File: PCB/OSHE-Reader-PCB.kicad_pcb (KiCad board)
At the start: 2 copper layers, 85 x 90 mm, 74 parts, among them J1 UART, J2 112L-TDA0, J3 JTAG, J5 boot_select, Q1 Si1308EDL, Q2 BSS138, Q3 BSS138, U1 74LVC1G04, U2 TPS923610DRLR, U3 TLV75533PDBV, U4 ESP32-S3-WROOM-1

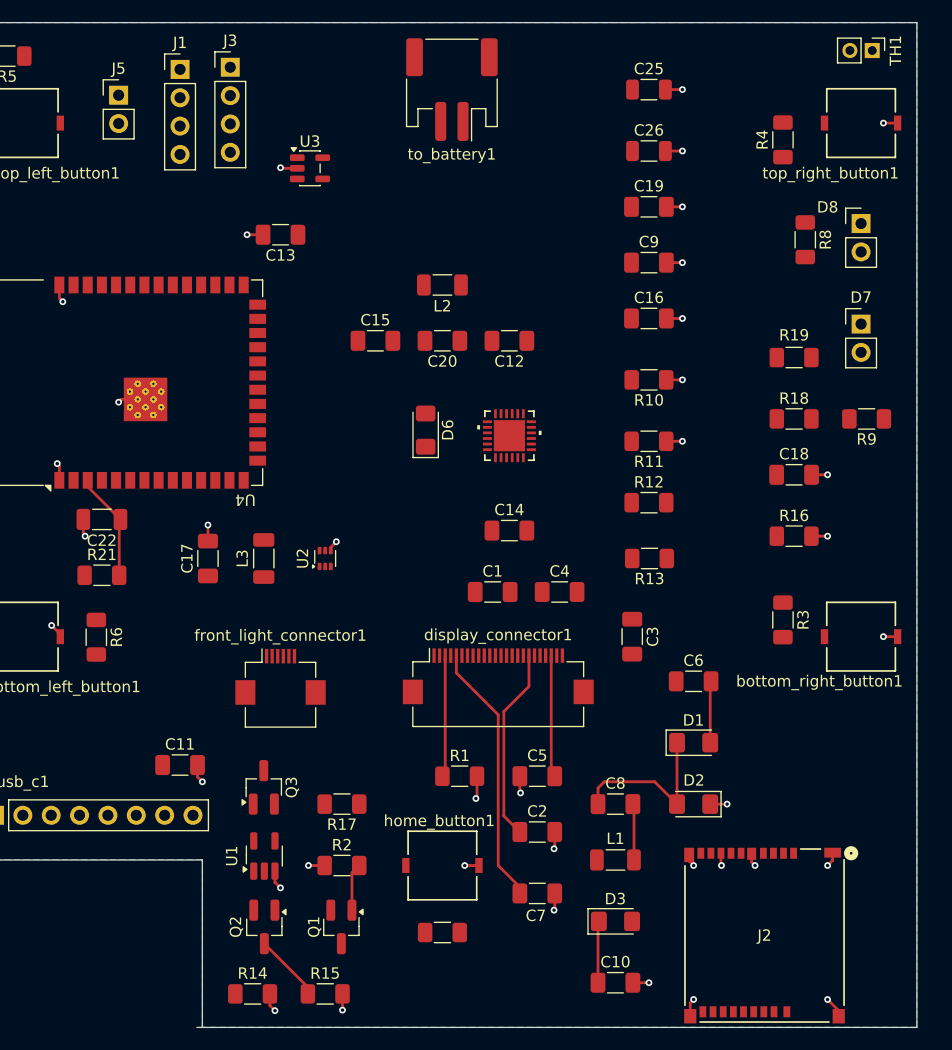
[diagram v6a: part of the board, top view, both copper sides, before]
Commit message: Did a bit more routing
Routed a bit more and placed components better
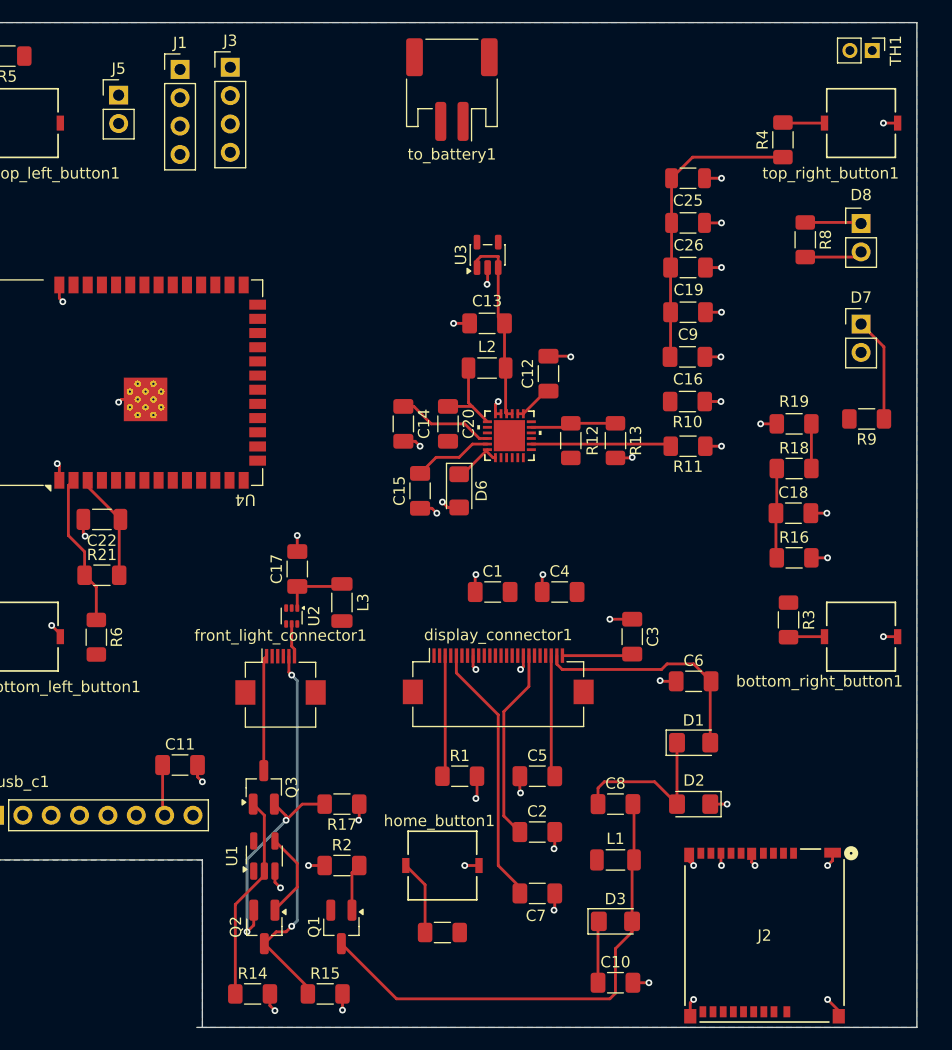
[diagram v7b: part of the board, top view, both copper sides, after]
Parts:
- D6: value D_Schottky_Small_Filled -> D_Schottky
- moved C13 20.1 mm to (115.0, 76.5)
- moved U3 17.7 mm to (115.0, 70.4), turned to 90 degrees
- moved C15 14.0 mm to (109.0, 91.5), turned to 90 degrees
- moved C14 13.5 mm to (107.5, 85.5), turned to -90 degrees
- moved R13 11.0 mm to (126.5, 87.0), turned to -90 degrees
- moved R12 8.94 mm to (122.5, 87.0), turned to 90 degrees
- moved C25 8.68 mm to (133.0, 63.5)
- moved L2 8.45 mm to (115.0, 80.5), turned to 0 degrees
- moved C17 8.06 mm to (98.0, 98.5)
- moved L3 8.03 mm to (102.0, 101.5), turned to -90 degrees
- moved C20 7.46 mm to (111.5, 85.5), turned to -90 degrees
- moved C26 7.33 mm to (133.0, 67.5)
- moved C19 6.47 mm to (133.0, 71.5)
- moved D6 6.21 mm to (112.5, 91.5), turned to -90 degrees
- moved U2 5.96 mm to (97.5, 102.7), turned to -90 degrees
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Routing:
- net +3V3: track 0.00 -> 40.5 mm
- net Net-(D3-A): track 5.04 -> 44.5 mm
- net /Display + Front Light/LED_C-: track 6.12 -> 33.9 mm, vias 0 -> 2
- net GND: track 56.8 -> 78.4 mm, vias 38 -> 51
- net /Display + Front Light/LED_C+: track 0.00 -> 21.4 mm
- net Net-(Q2-S): track 0.00 -> 19.6 mm, vias 0 -> 2
- net /Display + Front Light/COLOR_SEL: track 0.00 -> 18.5 mm
- net /Battery Charger/SYS: track 0.00 -> 17.6 mm
- net /Display + Front Light/VGL: track 5.53 -> 21.2 mm
- net Net-(battery_manager1-ILIM): track 0.00 -> 12.6 mm
- net Net-(D7-K): track 0.00 -> 9.35 mm
- net /VBUS: track 0.00 -> 9.10 mm
- net /Battery Charger/REGN: track 0.00 -> 8.72 mm
- net /Display + Front Light/COLOR_SEL_INV: track 0.00 -> 7.86 mm
- net /Battery Charger/TS: track 0.00 -> 7.68 mm
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
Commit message: Cutouts
Got cutouts working and added them for pivot points
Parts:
- moved J5 30.8 mm to (111.5, 65.0), turned to 90 degrees
- moved U4 28.8 mm to (95.6, 56.5), turned to 0 degrees
- moved J1 23.0 mm to (110.5, 53.0)
- moved J3 22.5 mm to (114.5, 53.0)
- moved D7 18.5 mm to (150.5, 95.0)
- moved to_battery1 14.2 mm to (126.0, 55.6)
- moved R9 11.7 mm to (146.0, 96.4), turned to -90 degrees
- moved C15 3.54 mm to (112.5, 92.0)
- moved D6 3.54 mm to (116.0, 92.0)
- moved C18 2.44 mm to (140.0, 93.5)
- moved R16 2.44 mm to (140.1, 97.5)
- moved R18 2.44 mm to (140.1, 89.5)
- moved R19 2.44 mm to (140.1, 85.5)
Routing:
- net /TL_button: track 0.00 -> 23.6 mm
- net /TMS: track 0.00 -> 12.1 mm, vias 0 -> 1
- net /TDI: track 0.00 -> 11.8 mm
- net /TDO: track 0.00 -> 11.0 mm
- net /TCK: track 0.00 -> 11.0 mm
- net Net-(D7-K): track 9.35 -> 0.00 mm
- net /RX: track 0.00 -> 6.89 mm
- net /TX: track 0.00 -> 6.40 mm
- net Net-(U4-EN): track 9.76 -> 5.05 mm
- net +3V3: track 40.5 -> 44.6 mm
- net Net-(battery_manager1-PMID): track 7.12 -> 4.56 mm
- net GND: track 78.4 -> 80.7 mm, vias 51 -> 52
- net /VBUS: track 9.10 -> 7.68 mm
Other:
- outline, holes or cut-outs redrawn
